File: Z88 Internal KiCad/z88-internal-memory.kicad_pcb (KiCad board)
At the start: 2 copper layers, 50.8 x 44.4 mm, 8 parts, among them J1 Conn_01x02, U1 M29F400, U2 IS61C5128AS-25TLI

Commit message: tweaks
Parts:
- added REF**: TestPoint_THTPad_D1.0mm_Drill0.5mm, TestPoint:TestPoint_THTPad_D1.0mm_Drill0.5mm, F.Cu at (109.8, 88.9)
- added REF**: TestPoint_THTPad_D1.0mm_Drill0.5mm, TestPoint:TestPoint_THTPad_D1.0mm_Drill0.5mm, F.Cu at (107.3, 88.9)
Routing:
- net /A18: track 35.4 -> 61.3 mm, vias 2 -> 3
- net /A17: track 30.4 -> 53.3 mm
- net /D1: track 52.5 -> 49.7 mm, vias 1 -> 0
- net /D2: track 54.2 -> 51.4 mm, vias 1 -> 0
- net /D0: track 50.5 -> 47.7 mm, vias 1 -> 0
- net /D7: track 63.0 -> 60.6 mm, vias 2 -> 0
- net /D4: track 62.1 -> 59.8 mm, vias 2 -> 0
- net /D5: track 62.3 -> 60.1 mm, vias 2 -> 0
- net /D6: track 62.4 -> 60.3 mm, vias 2 -> 0
- net /A1: track 44.9 -> 43.1 mm
- net /A0: track 56.7 -> 54.9 mm, vias 3 -> 2
- net /A16: track 49.8 -> 51.1 mm
- net /A14: track 51.2 -> 52.5 mm
- net /A12: track 35.0 -> 36.3 mm
- net /A8: track 54.4 -> 55.5 mm
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
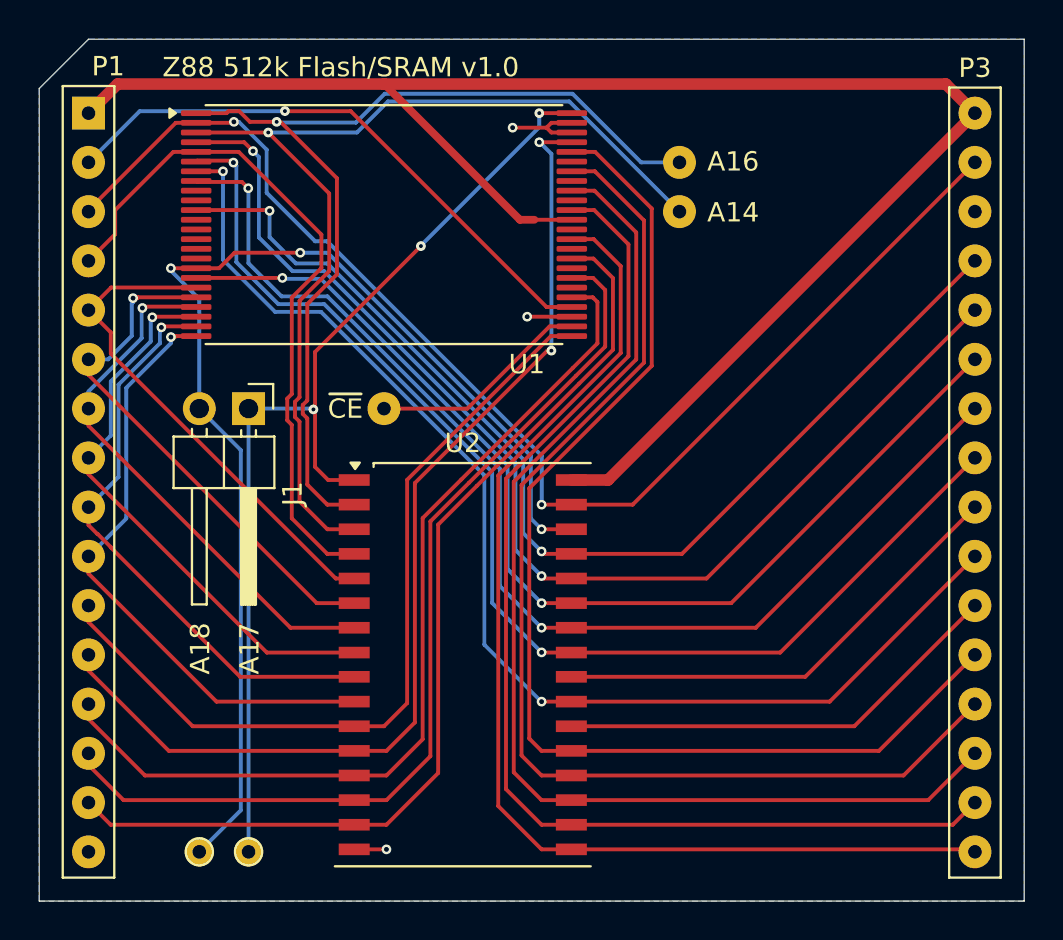
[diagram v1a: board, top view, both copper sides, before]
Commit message: updated silkscreen
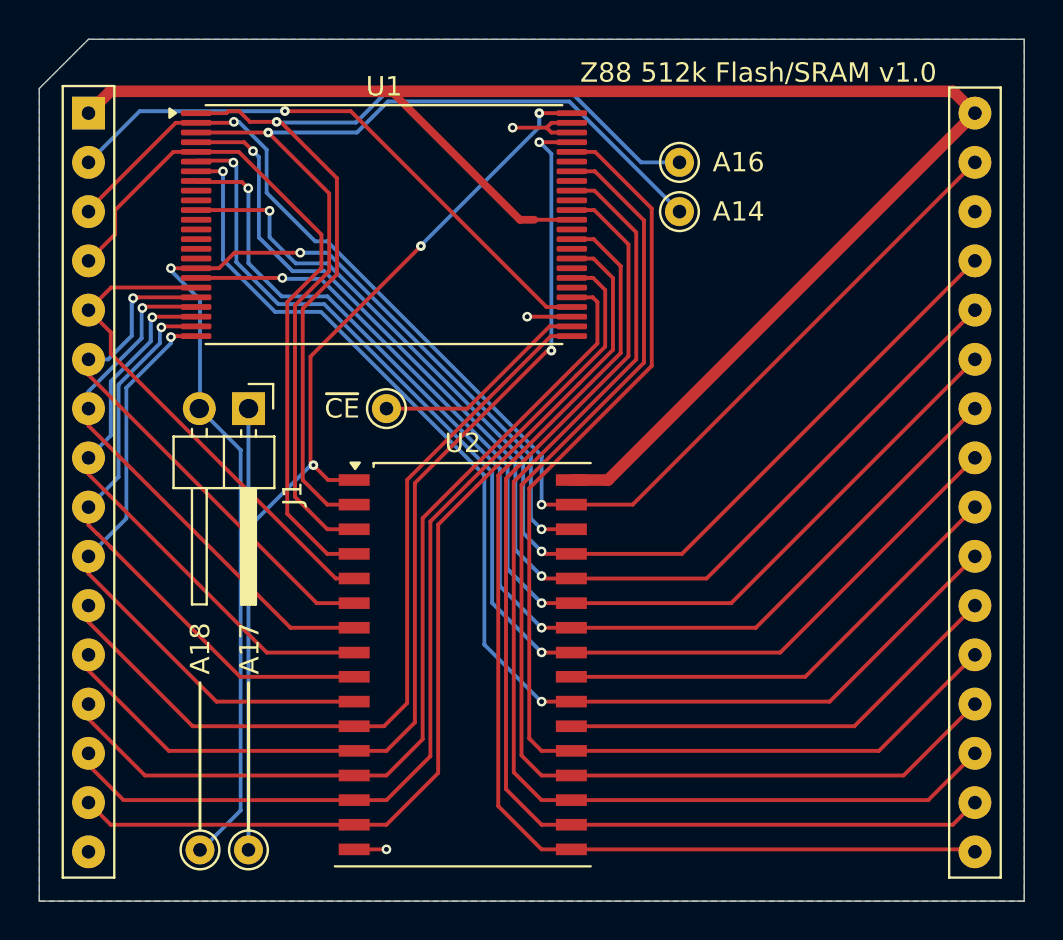
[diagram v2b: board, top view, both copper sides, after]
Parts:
- removed REF** (x2): TestPoint_THTPad_D1.0mm_Drill0.5mm, TestPoint:TestPoint_THTPad_D1.0mm_Drill0.5mm
- added TP4: TestPoint, Z88 internal memory:TestPoint, F.Cu at (109.8, 88.8)
- added TP5: TestPoint, Z88 internal memory:TestPoint, F.Cu at (107.3, 88.8)
- moved TP1 0.13 mm to (116.9, 66.0)
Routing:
- net /A17: track 53.3 -> 54.8 mm
- net VCC: track 88.2 -> 87.4 mm

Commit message: layout tweaks, added correct machined-pin headers
3D model and new footprint for pin headers, with silkscreening for back of board mounting
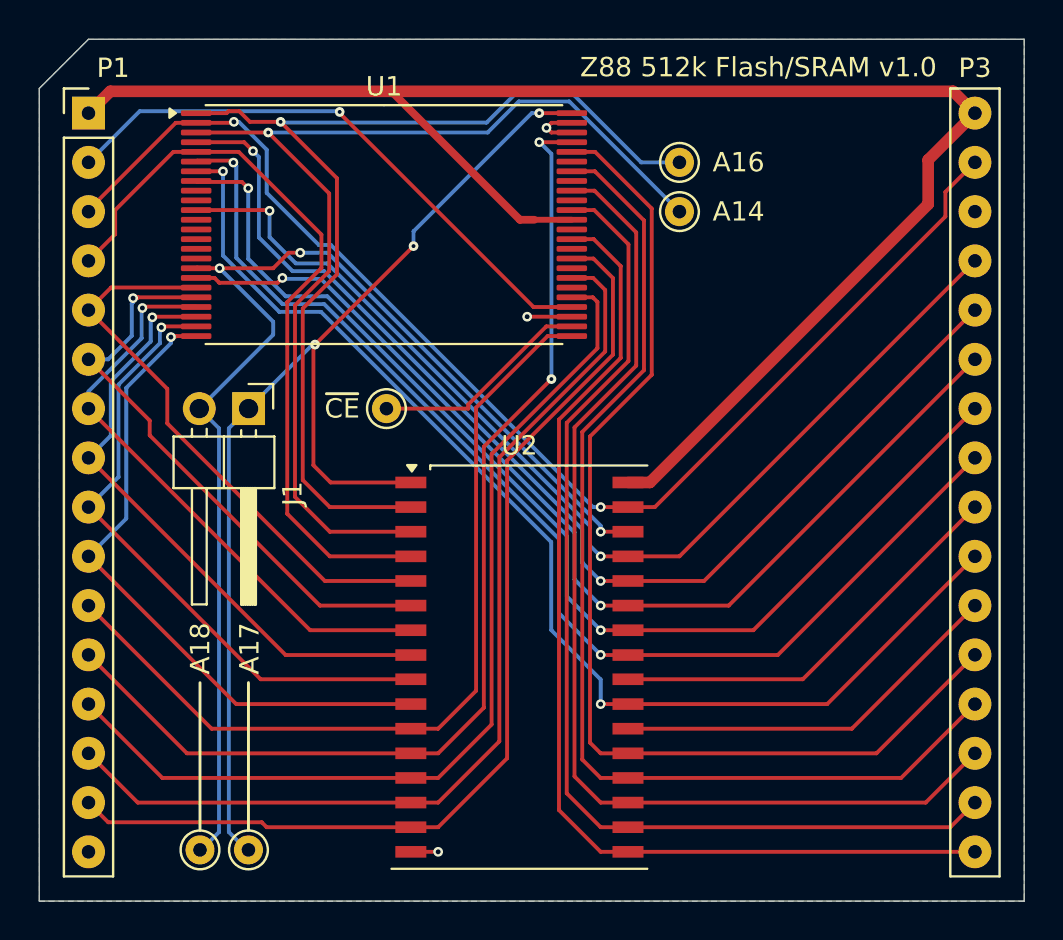
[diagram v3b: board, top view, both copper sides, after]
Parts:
- P1: footprint Package_DIP_Custom:DIP-32_W_Left -> Connector_SIP_Header:SIPHeader_1x16_Vertical_P1; moved to B.Cu
- P3: footprint Package_DIP_Custom:DIP-32_W_Right -> Connector_SIP_Header:SIPHeader_1x16_Vertical; moved to B.Cu
- moved P3 15.2 mm to (147.3, 50.8), turned to 180 degrees
- moved U2 2.92 mm to (123.8, 79.4)
- turned P1 to 180 degrees
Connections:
- net Net-(P1A-~{ROE}) renamed /~{ROE}
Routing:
- net /D3: track 59.1 -> 54.8 mm
- net /D5: track 60.1 -> 55.9 mm
- net /D4: track 59.8 -> 55.6 mm
- net /D7: track 60.6 -> 56.4 mm
- net /D6: track 60.3 -> 56.1 mm
- net /A17: track 54.8 -> 58.8 mm
- net /A7: track 26.1 -> 29.5 mm
- net /A14: track 52.5 -> 55.5 mm
- net /A12: track 36.3 -> 39.3 mm
- net /A6: track 27.4 -> 30.3 mm
- net /~{OE}: track 24.4 -> 21.6 mm
- net /~{CS1}: track 23.4 -> 20.5 mm
- net /A16: track 51.1 -> 53.9 mm
- net /A4: track 29.2 -> 31.7 mm
- net /A5: track 28.1 -> 30.5 mm
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
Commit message: added bypass caps, pre-production tweaks
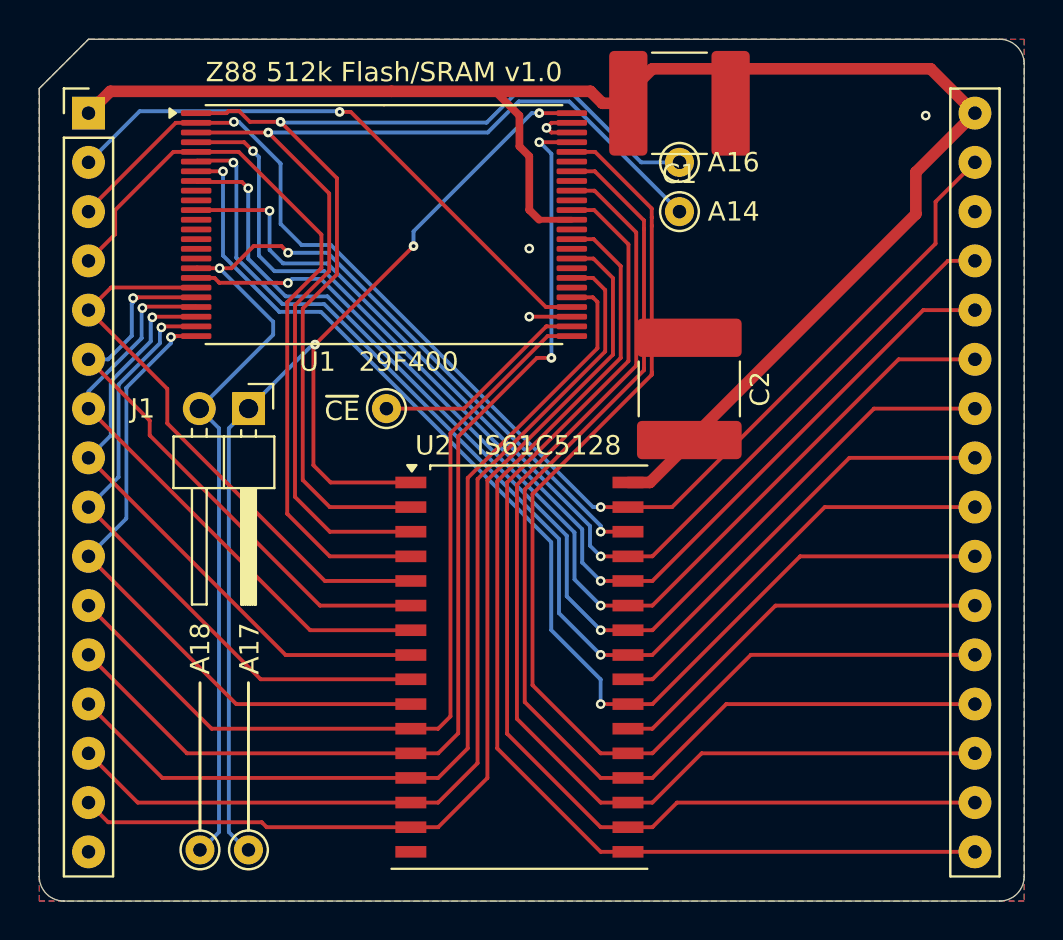
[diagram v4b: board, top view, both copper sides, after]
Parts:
- added C1: 100 nF, Capacitor_SMD:C_2220_5750Metric_Pad1.97x5.40mm_HandSolder, F.Cu at (132.0, 50.3)
- added C2: 100 nF, Capacitor_SMD:C_2220_5750Metric_Pad1.97x5.40mm_HandSolder, F.Cu at (132.6, 65.0)
- U1: value M29F400 -> 29F400
- U2: value IS61C5128AS-25TLI -> IS61C5128
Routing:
- net /D3: track 54.8 -> 57.5 mm
- net /D4: track 55.6 -> 58.1 mm
- net /D6: track 56.1 -> 58.6 mm
- net /D7: track 56.4 -> 58.8 mm
- net /D5: track 55.9 -> 58.3 mm
- net GND: track 6.72 -> 5.20 mm, vias 3 -> 4
- net /A15: track 65.3 -> 66.4 mm
- net /A13: track 58.8 -> 59.3 mm
- added copper zone on F.Cu, net GND
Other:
- outline, holes or cut-outs redrawn
